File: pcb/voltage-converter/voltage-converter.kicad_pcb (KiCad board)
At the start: 2 copper layers, 22.4 x 52.4 mm, 20 parts, among them J4 Conn_01x02, J8 I2C, U3 R-78C3.3-1.0

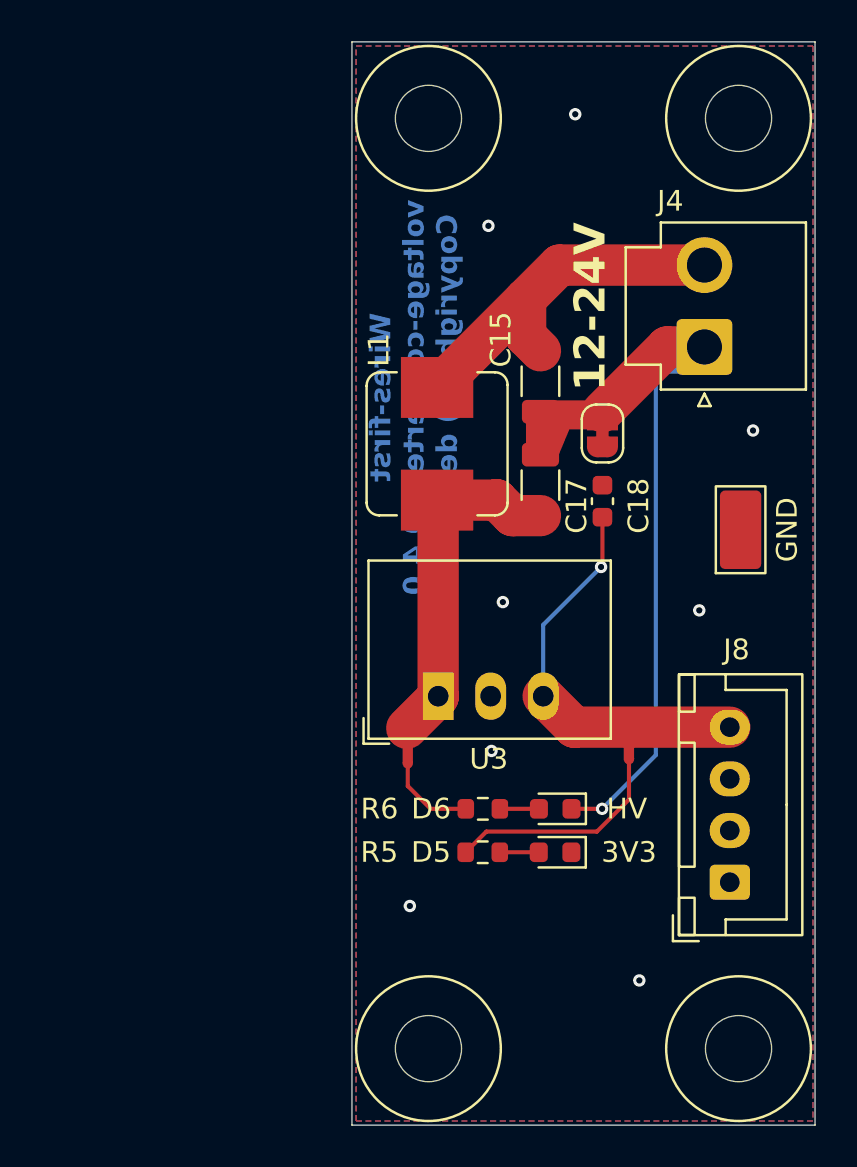
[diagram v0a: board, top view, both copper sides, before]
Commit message: Making converter PCB larger.
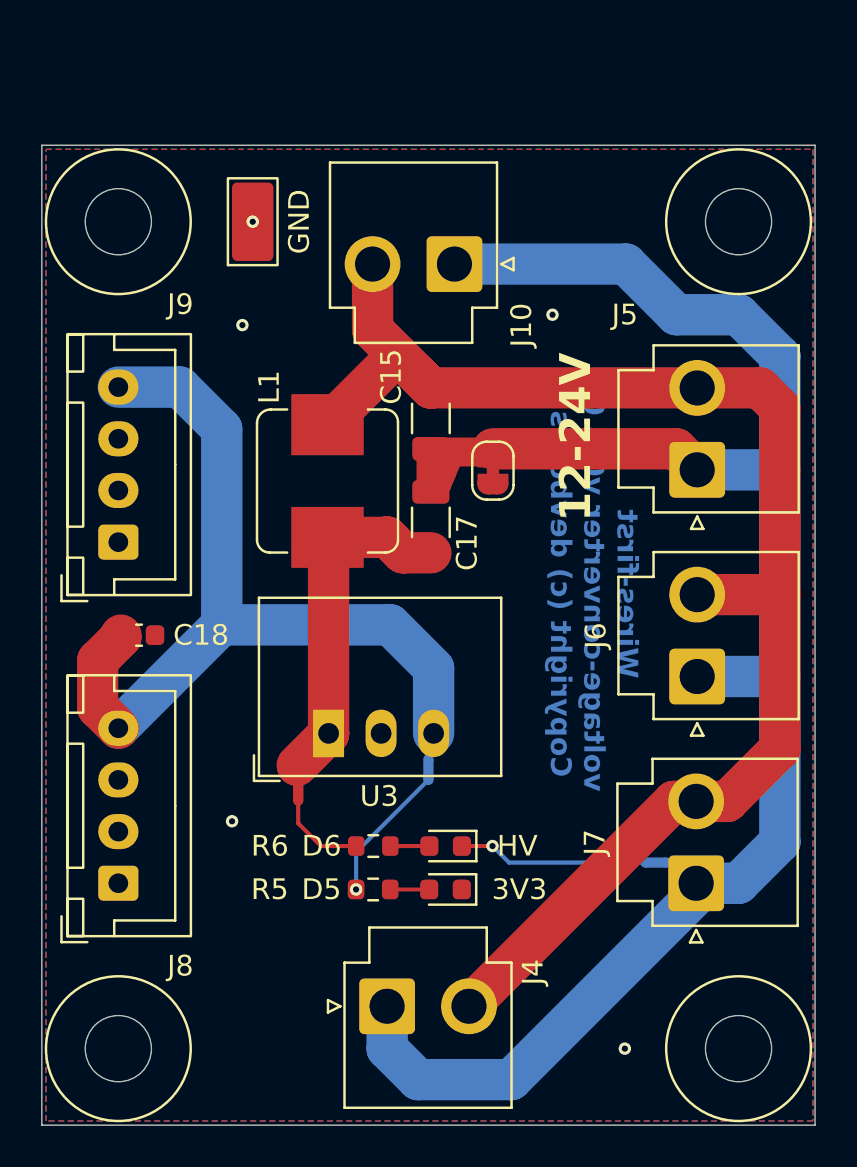
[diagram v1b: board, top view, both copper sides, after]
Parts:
- added J10: Conn_01x02, Connector_JST:JST_VH_B2P-VH_1x02_P3.96mm_Vertical, F.Cu at (96.3, 102.0)
- added J5: Conn_01x02, Connector_JST:JST_VH_B2P-VH_1x02_P3.96mm_Vertical, F.Cu at (108.0, 112.0)
- added J6: Conn_01x02, Connector_JST:JST_VH_B2P-VH_1x02_P3.96mm_Vertical, F.Cu at (108.0, 122.0)
- added J7: Conn_01x02, Connector_JST:JST_VH_B2P-VH_1x02_P3.96mm_Vertical, F.Cu at (108.0, 132.0)
- added J9: I2C, Connector_JST:JST_XH_B4B-XH-A_1x04_P2.50mm_Vertical, F.Cu at (80.0, 115.5)
- NT4: moved to B.Cu
- moved J4 35.4 mm to (93.0, 137.9), turned to 0 degrees
- moved J8 29.6 mm to (80.0, 132.0)
- moved TP1 27.9 mm to (86.5, 100.0)
- moved NT3 23.9 mm to (106.0, 131.0)
- moved C18 23.3 mm to (81.0, 120.0), turned to 0 degrees
- moved H1 15.8 mm to (80.0, 100.0)
- moved H3 15.0 mm to (80.0, 140.0)
- moved NT4 9.75 mm to (95.0, 126.5)
- moved D5 5.60 mm to (95.8, 132.3)
- moved R5 5.60 mm to (92.3, 132.3)
- moved C15 5.60 mm to (95.1, 109.5)
- moved C17 5.60 mm to (95.1, 114.5)
- moved JP1 5.60 mm to (98.1, 112.0)
- moved L1 5.60 mm to (90.1, 112.5)
- moved NT2 5.60 mm to (88.7, 127.5)
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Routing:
- net HV-GND: track 6.23 -> 86.1 mm
- net /hv-in-1: track 19.1 -> 71.9 mm
- net 3V3: track 19.5 -> 45.5 mm, vias 1 -> 0
- net Net-(D6-K): track 23.9 -> 9.21 mm
- net Net-(NT4-Pad1): track 10.9 -> 6.75 mm, vias 0 -> 1
- net GND: vias 8 -> 5
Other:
- board size 22.4 x 52.4 mm -> 37.4 x 47.4 mm

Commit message: Preparing voltage converter for fabrication.
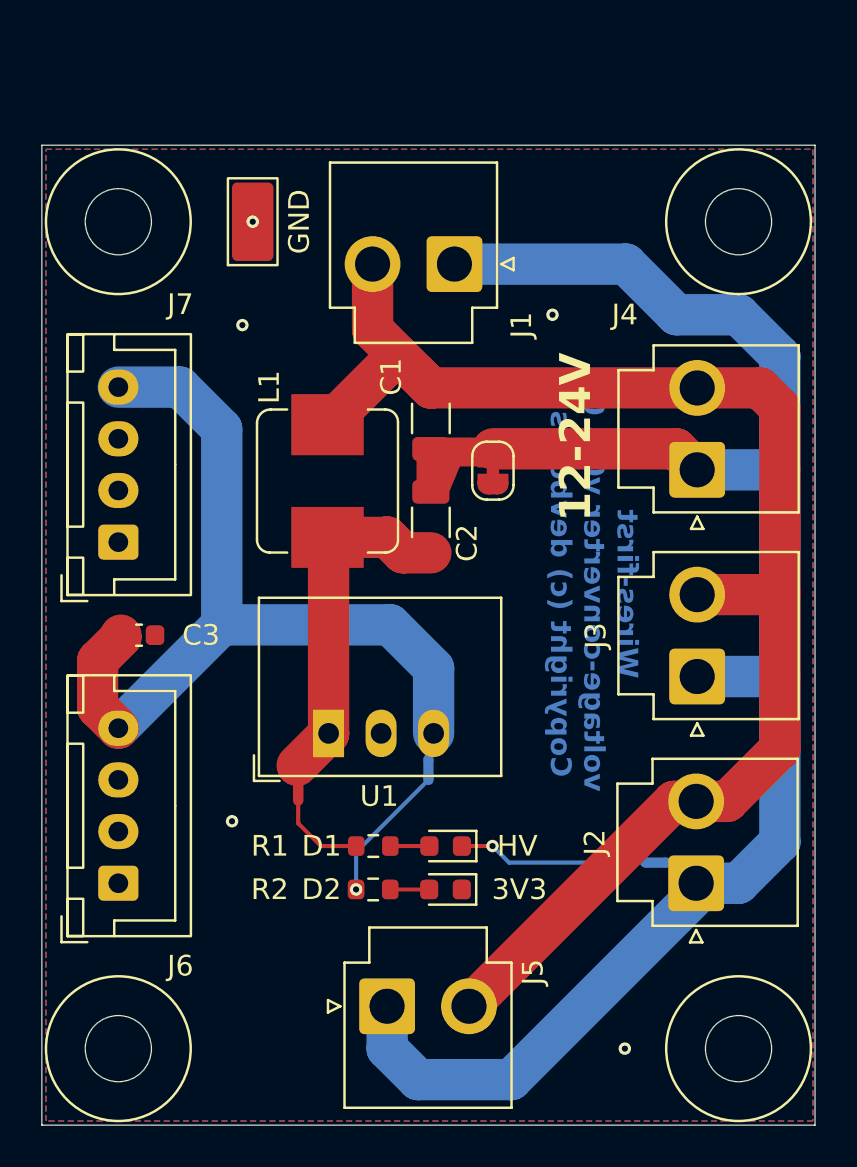
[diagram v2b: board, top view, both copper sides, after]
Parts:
- J6: renamed from J8; value I2C -> ~
- J7: renamed from J9; value I2C -> ~
- renumbered C15 to C1, C17 to C2, C18 to C3, D6 to D1, D5 to D2, J10 to J1, J7 to J2, J6 to J3, J5 to J4, J4 to J5, NT2 to NT1, NT3 to NT2, NT4 to NT3, R6 to R1, R5 to R2, U3 to U1
